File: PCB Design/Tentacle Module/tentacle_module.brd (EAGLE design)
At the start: 94 x 50.8 mm, 49 parts, among them IC1 5V, T1 NTD5867NL, T2 NTD5867NL, T3 NTD5867NL, T4 NTD5867NL, X3 RJ45-8X, X4 RJ45-8X

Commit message: Added the RJ45 connector
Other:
- outline, holes or cut-outs redrawn
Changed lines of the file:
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@@
 <board>
 <plain>
-<wire x1="0" y1="0" x2="93.98" y2="0" width="0.6096" layer="20"/>
+<wire x1="0" y1="0" x2="16.51" y2="0" width="0.6096" layer="20"/>
+<wire x1="16.51" y1="0" x2="38.1" y2="0" width="0.6096" layer="20"/>
+<wire x1="38.1" y1="0" x2="93.98" y2="0" width="0.6096" layer="20"/>
 <wire x1="93.98" y1="0" x2="93.98" y2="50.8" width="0.6096" layer="20"/>
 <wire x1="93.98" y1="50.8" x2="0" y2="50.8" width="0.6096" layer="20"/>
@@
 <hole x="80.01" y="3.175" drill="4.7625"/>
 <hole x="12.7" y="3.175" drill="4.7625"/>
+<wire x1="16.51" y1="0" x2="16.51" y2="21.59" width="0.4064" layer="20"/>
+<wire x1="16.51" y1="21.59" x2="38.1" y2="21.59" width="0.4064" layer="20"/>
+<wire x1="38.1" y1="21.59" x2="38.1" y2="0" width="0.4064" layer="20"/>
 </plain>
 <attributes>

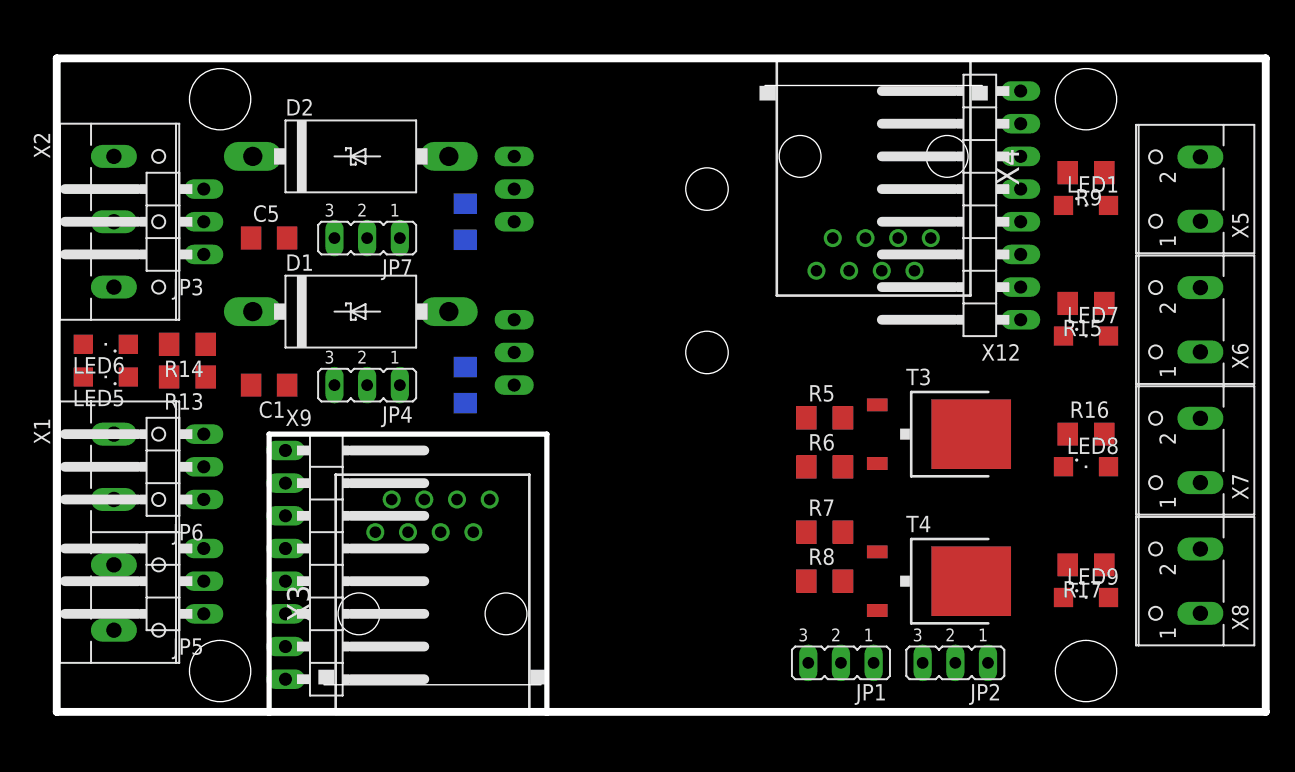
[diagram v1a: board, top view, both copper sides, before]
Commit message: Routed the RJ45 connector with side and top headers
Also added the accelerometer chip to the library
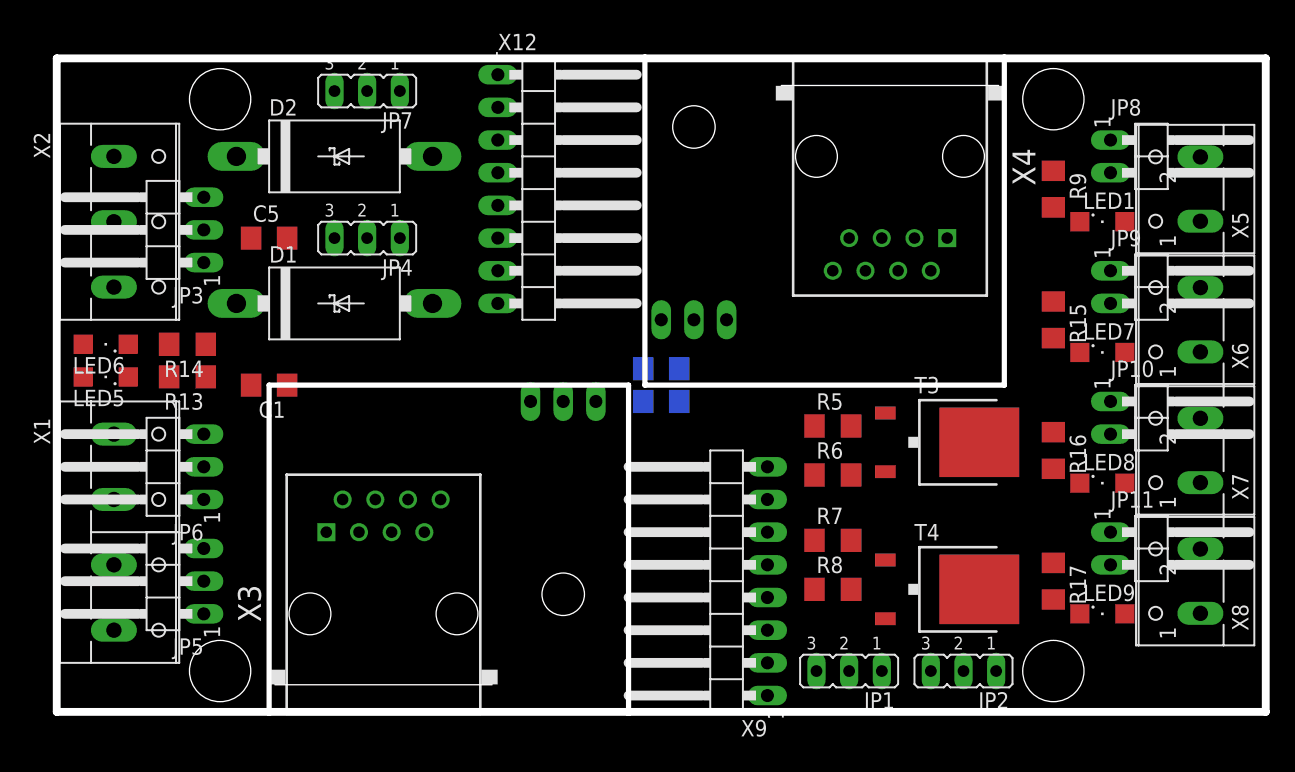
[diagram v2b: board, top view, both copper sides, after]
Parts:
- added JP10, JP11, JP8, JP9: (no value), CBLA_Test_bed_Library:1X02/90
- JP3, JP5, JP6: device pinhead:1X03/90 -> CBLA_Test_bed_Library:1X03/90
- X12, X9: device pinhead:1X08/90 -> CBLA_Test_bed_Library:1X08/90
- moved X12 33.0 mm to (38.1, 40.6), turned to 270 degrees
- moved X9 29.9 mm to (51.4, 10.2), turned to 90 degrees
- moved C4 19.1 mm to (47.0, 26.7), turned to 180 degrees
- moved C2 15.3 mm to (47.0, 24.1), turned to 0 degrees
- moved IC2 12.0 mm to (49.5, 34.3), turned to 0 degrees
- moved JP4 11.4 mm to (24.1, 36.8)
- moved JP7 11.4 mm to (24.1, 48.3)
- moved IC1 7.62 mm to (39.4, 20.3), turned to 180 degrees
- moved X3 3.81 mm to (25.4, 7.62)
- moved R15 2.84 mm to (77.5, 30.5), turned to 270 degrees
- moved R16 2.84 mm to (77.5, 20.3), turned to 270 degrees
- moved R17 2.84 mm to (77.5, 10.2), turned to 270 degrees
- moved R9 2.84 mm to (77.5, 40.6), turned to 270 degrees
- moved LED9 1.80 mm to (81.3, 7.62)
- moved LED7 1.80 mm to (81.3, 27.9)
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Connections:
- net +5V_HI-PWR: now also JP10.1, JP11.1, JP8.1, JP9.1
- net SMA1_OUT-: now also JP8.2
- net SMA2_OUT-: now also JP9.2
- net SMA3_OUT-: now also JP10.2
- net SMA4_OUT-: now also JP11.2
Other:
- outline, holes or cut-outs redrawn

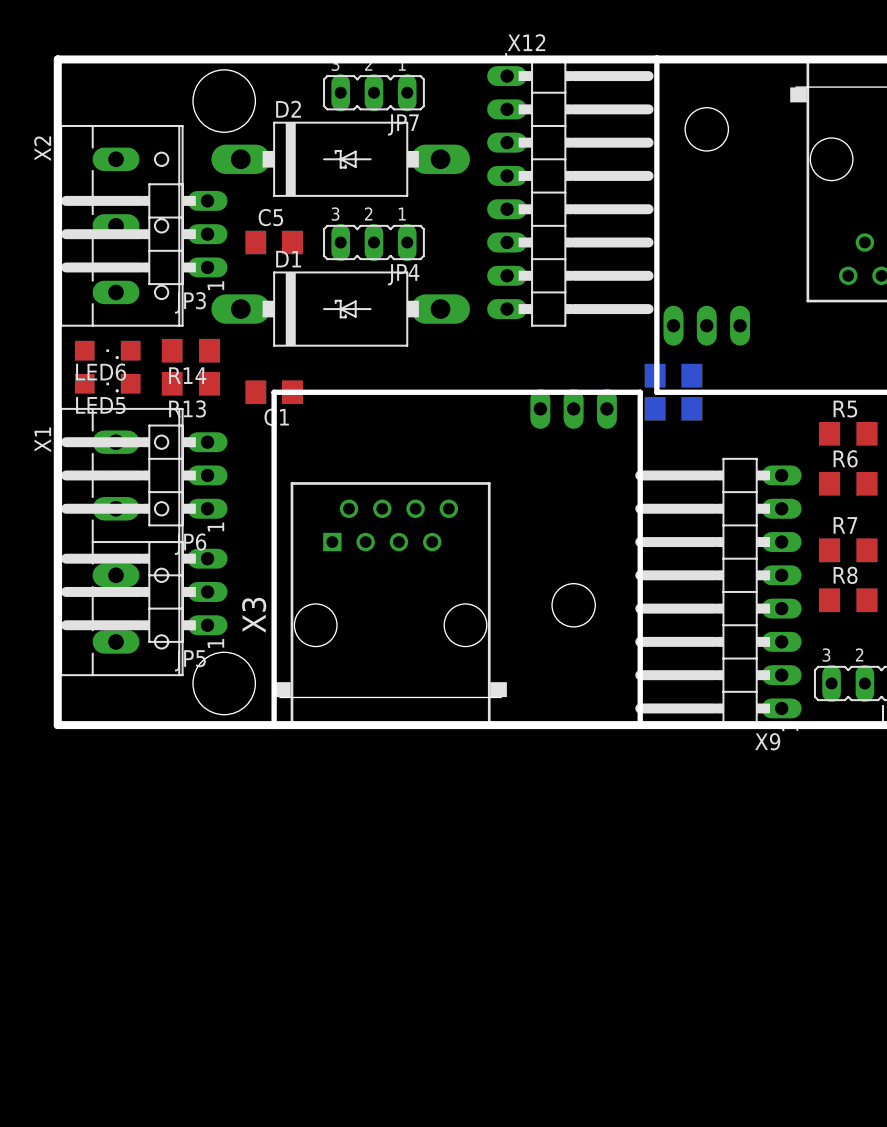
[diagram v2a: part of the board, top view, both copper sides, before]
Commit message: Changed location of the header to make it much easier to router
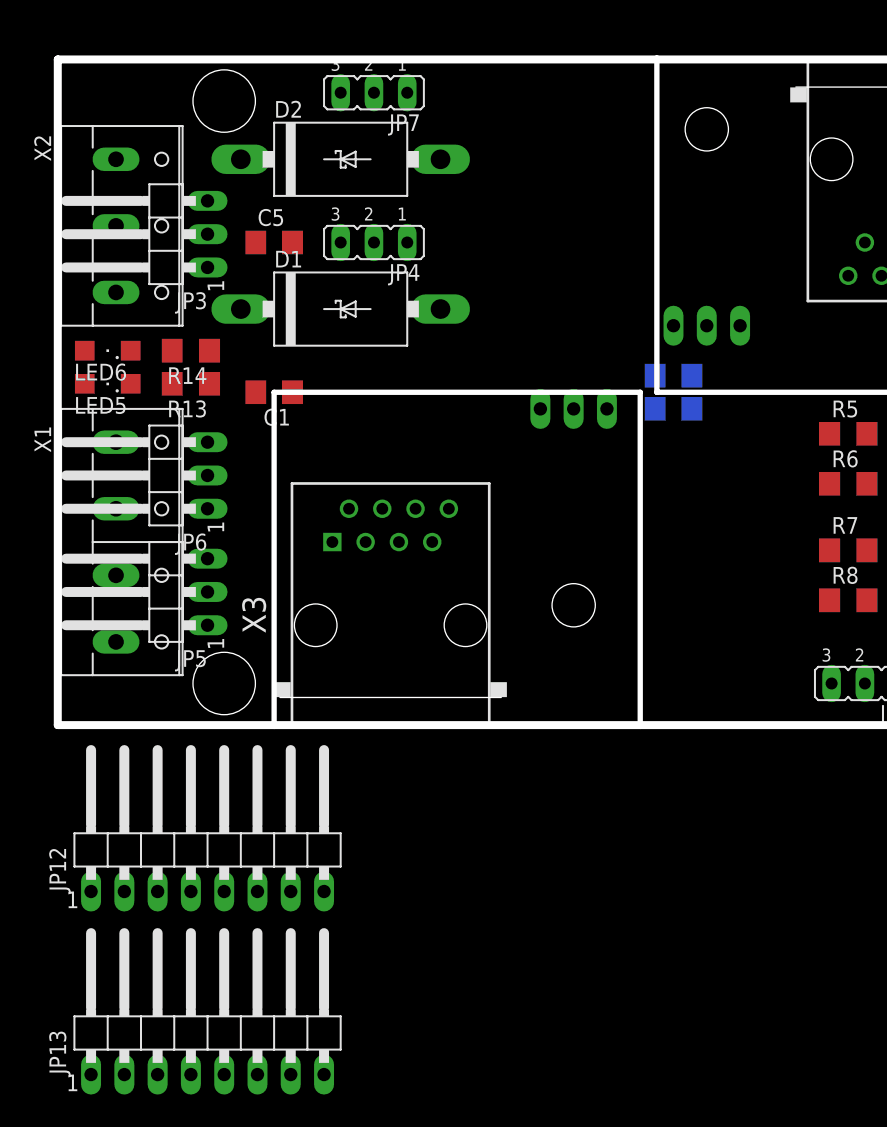
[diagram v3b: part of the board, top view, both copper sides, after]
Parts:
- removed X12, X9: (no value), CBLA_Test_bed_Library:1X08/90
- added JP12, JP13: (no value), CBLA_Test_bed_Library:1X08/90
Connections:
- net +3.3V: now also JP13.8; no longer X12.1
- net +5V: now also JP13.6; no longer X12.3
- net GND: now also JP13.7; no longer X12.2
- net IR1: now also JP12.4; no longer X9.5
- net IR2: now also JP12.3, JP13.5; no longer X12.4, X9.6
- net PWM1: now also JP12.8; no longer X9.1
- net PWM2: now also JP12.7; no longer X9.2
- net PWM3: now also JP12.6; no longer X9.3
- net PWM4: now also JP12.5; no longer X9.4
- net SCL: now also JP12.2, JP13.3; no longer X12.6, X9.7
- net SDA: now also JP12.1, JP13.4; no longer X12.5, X9.8
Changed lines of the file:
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@@
 <element name="T3" library="CBLA_Test_bed_Library" package="DPACK" value="NTD5867NL" x="69.215" y="20.955" rot="R270"/>
 <element name="T4" library="CBLA_Test_bed_Library" package="DPACK" value="NTD5867NL" x="69.215" y="9.525" rot="R270"/>
-<element name="X12" library="CBLA_Test_bed_Library" package="1X08/90" value="" x="38.1" y="40.64" rot="R270"/>
 <element name="X2" library="con-wago-508" package="W237-133" value="" x="5.08" y="38.1" rot="R270">
 <attribute name="OC_NEWARK" value="unknown" x="5.08" y="38.1" size="1.778" layer="27" rot="R270" display="off"/>
@@
 <attribute name="OC_FARNELL" value="unknown" x="87.63" y="10.16" size="1.778" layer="27" rot="R90" display="off"/>
 </element>
-<element name="X9" library="CBLA_Test_bed_Library" package="1X08/90" value="" x="51.435" y="10.16" rot="R90"/>
 <element name="X1" library="con-wago-508" package="W237-4P" value="" x="5.08" y="13.97" rot="R270">
 <attribute name="OC_NEWARK" value="unknown" x="5.08" y="13.97" size="1.778" layer="27" rot="R270" display="off"/>
@@
 <element name="JP10" library="CBLA_Test_bed_Library" package="1X02/90" value="" x="85.725" y="22.86" rot="R270"/>
 <element name="JP11" library="CBLA_Test_bed_Library" package="1X02/90" value="" x="85.725" y="12.7" rot="R270"/>
+<element name="JP12" library="CBLA_Test_bed_Library" package="1X08/90" value="" x="11.43" y="-8.89"/>
+<element name="JP13" library="CBLA_Test_bed_Library" package="1X08/90" value="" x="11.43" y="-22.86"/>
 </elements>
 <signals>
@@
 <contactref element="JP2" pad="3"/>
 <contactref element="JP1" pad="2"/>
-<contactref element="X12" pad="3"/>
+<contactref element="JP13" pad="6"/>
 <wire x1="48.39" y1="24.13" x2="66.675" y2="36.83" width="0" layer="19" extent="16-16"/>
 <wire x1="41.91" y1="24.13" x2="48.39" y2="24.13" width="0" layer="19" extent="16-16"/>
-<wire x1="34.29" y1="44.45" x2="41.91" y2="24.13" width="0" layer="19" extent="1-1"/>
 <wire x1="61.595" y1="3.175" x2="48.39" y2="24.13" width="0" layer="19" extent="16-16"/>
 <wire x1="67.945" y1="3.175" x2="61.595" y2="3.175" width="0" layer="19" extent="1-1"/>
 <wire x1="73.025" y1="3.175" x2="67.945" y2="3.175" width="0" layer="19" extent="1-1"/>
+<wire x1="15.24" y1="-26.67" x2="61.595" y2="3.175" width="0" layer="19" extent="1-1"/>
 </signal>
 <signal name="+3V3">
@@
 <contactref element="X3" pad="1"/>
 <contactref element="R3" pad="1"/>
-<contactref element="X9" pad="1"/>
-<wire x1="55.245" y1="1.27" x2="58.903" y2="22.225" width="0" layer="19" extent="16-16"/>
-<wire x1="20.955" y1="13.97" x2="55.245" y2="1.27" width="0" layer="19" extent="1-1"/>
+<contactref element="JP12" pad="8"/>
+<wire x1="20.955" y1="13.97" x2="58.903" y2="22.225" width="0" layer="19" extent="16-16"/>
+<wire x1="20.32" y1="-12.7" x2="20.955" y2="13.97" width="0" layer="19" extent="1-1"/>
 </signal>
 <signal name="PWM2">
 <contactref element="X3" pad="2"/>
 <contactref element="R4" pad="1"/>
-<contactref element="X9" pad="2"/>
-<wire x1="55.245" y1="3.81" x2="58.903" y2="13.335" width="0" layer="19" extent="16-16"/>
-<wire x1="22.225" y1="16.51" x2="55.245" y2="3.81" width="0" layer="19" extent="1-1"/>
+<contactref element="JP12" pad="7"/>
+<wire x1="22.225" y1="16.51" x2="58.903" y2="13.335" width="0" layer="19" extent="16-16"/>
+<wire x1="17.78" y1="-12.7" x2="22.225" y2="16.51" width="0" layer="19" extent="1-1"/>
 </signal>
 <signal name="PWM3">
 <contactref element="X3" pad="3"/>
-<contactref element="X9" pad="3"/>
 <contactref element="R6" pad="1"/>
-<wire x1="55.245" y1="6.35" x2="58.903" y2="18.415" width="0" layer="19" extent="1-1"/>
-<wire x1="23.495" y1="13.97" x2="55.245" y2="6.35" width="0" layer="19" extent="1-1"/>
+<contactref element="JP12" pad="6"/>
+<wire x1="23.495" y1="13.97" x2="58.903" y2="18.415" width="0" layer="19" extent="1-1"/>
+<wire x1="15.24" y1="-12.7" x2="23.495" y2="13.97" width="0" layer="19" extent="1-1"/>
 </signal>
 <signal name="PWM4">
 <contactref element="X3" pad="4"/>
-<contactref element="X9" pad="4"/>
 <contactref element="R8" pad="1"/>
-<wire x1="55.245" y1="8.89" x2="58.903" y2="9.525" width="0" layer="19" extent="1-1"/>
-<wire x1="24.765" y1="16.51" x2="55.245" y2="8.89" width="0" layer="19" extent="1-1"/>
+<contactref element="JP12" pad="5"/>
+<wire x1="24.765" y1="16.51" x2="58.903" y2="9.525" width="0" layer="19" extent="1-1"/>
+<wire x1="12.7" y1="-12.7" x2="24.765" y2="16.51" width="0" layer="19" extent="1-1"/>
 </signal>
 <signal name="IR1">
 <contactref element="X3" pad="5"/>
-<contactref element="X9" pad="5"/>
-<wire x1="26.035" y1="13.97" x2="55.245" y2="11.43" width="0" layer="19" extent="1-1"/>
+<contactref element="JP12" pad="4"/>
+<wire x1="10.16" y1="-12.7" x2="26.035" y2="13.97" width="0" layer="19" extent="1-1"/>
 </signal>
 <signal name="IR2">
 <contactref element="X3" pad="6"/>
 <contactref element="X4" pad="4"/>
-<contactref element="X9" pad="6"/>
-<contactref element="X12" pad="4"/>
-<wire x1="55.245" y1="13.97" x2="65.405" y2="34.29" width="0" layer="19" extent="1-1"/>
-<wire x1="27.305" y1="16.51" x2="55.245" y2="13.97" width="0" layer="19" extent="1-1"/>
-<wire x1="34.29" y1="41.91" x2="65.405" y2="34.29" width="0" layer="19" extent="1-1"/>
+<contactref element="JP12" pad="3"/>
+<contactref element="JP13" pad="5"/>
+<wire x1="27.305" y1="16.51" x2="65.405" y2="34.29" width="0" layer="19" extent="1-1"/>
+<wire x1="7.62" y1="-12.7" x2="27.305" y2="16.51" width="0" layer="19" extent="1-1"/>
+<wire x1="12.7" y1="-26.67" x2="7.62" y2="-12.7" width="0" layer="19" extent="1-1"/>
 </signal>
 <signal name="SCL">
 <contactref element="X3" pad="7"/>
 <contactref element="X4" pad="6"/>
-<contactref element="X9" pad="7"/>
-<contactref element="X12" pad="6"/>
-<wire x1="55.245" y1="16.51" x2="62.865" y2="34.29" width="0" layer="19" extent="1-1"/>
-<wire x1="28.575" y1="13.97" x2="55.245" y2="16.51" width="0" layer="19" extent="1-1"/>
-<wire x1="34.29" y1="36.83" x2="55.245" y2="16.51" width="0" layer="19" extent="1-1"/>
+<contactref element="JP12" pad="2"/>
+<contactref element="JP13" pad="3"/>
+<wire x1="28.575" y1="13.97" x2="62.865" y2="34.29" width="0" layer="19" extent="1-1"/>
+<wire x1="5.08" y1="-12.7" x2="28.575" y2="13.97" width="0" layer="19" extent="1-1"/>
+<wire x1="7.62" y1="-26.67" x2="5.08" y2="-12.7" width="0" layer="19" extent="1-1"/>
 </signal>
 <signal name="SDA">
 <contactref element="X3" pad="8"/>
 <contactref element="X4" pad="5"/>
-<contactref element="X9" pad="8"/>
-<contactref element="X12" pad="5"/>
-<wire x1="55.245" y1="19.05" x2="64.135" y2="36.83" width="0" layer="19" extent="1-1"/>
-<wire x1="29.845" y1="16.51" x2="55.245" y2="19.05" width="0" layer="19" extent="1-1"/>
-<wire x1="34.29" y1="39.37" x2="55.245" y2="19.05" width="0" layer="19" extent="1-1"/>
+<contactref element="JP12" pad="1"/>
+<contactref element="JP13" pad="4"/>
+<wire x1="29.845" y1="16.51" x2="64.135" y2="36.83" width="0" layer="19" extent="1-1"/>
+<wire x1="2.54" y1="-12.7" x2="29.845" y2="16.51" width="0" layer="19" extent="1-1"/>
+<wire x1="10.16" y1="-26.67" x2="2.54" y2="-12.7" width="0" layer="19" extent="1-1"/>
 </signal>
 <signal name="+3.3V">
 <contactref element="X4" pad="1"/>
-<contactref element="X12" pad="1"/>
-<wire x1="34.29" y1="49.53" x2="69.215" y2="36.83" width="0" layer="19" extent="1-1"/>
+<contactref element="JP13" pad="8"/>
+<wire x1="20.32" y1="-26.67" x2="69.215" y2="36.83" width="0" layer="19" extent="1-1"/>
 </signal>
 <signal name="GND">
@@
 <contactref element="JP5" pad="2"/>
 <contactref element="JP6" pad="2"/>
-<contactref element="X12" pad="2"/>
 <contactref element="X1" pad="2"/>
 <contactref element="X1" pad="3"/>
+<contactref element="JP13" pad="7"/>
 <wire x1="64.415" y1="23.235" x2="67.945" y2="34.29" width="0" layer="19" extent="16-16"/>
 <wire x1="64.415" y1="18.675" x2="64.415" y2="23.235" width="0" layer="19" extent="1-16"/>
@@
 <wire x1="64.415" y1="7.245" x2="64.415" y2="11.805" width="0" layer="19" extent="1-16"/>
 <wire x1="48.39" y1="26.67" x2="58.903" y2="22.225" width="0" layer="19" extent="1-16"/>
+<wire x1="45.59" y1="24.13" x2="48.39" y2="26.67" width="0" layer="19" extent="16-16"/>
 <wire x1="49.53" y1="30.48" x2="48.39" y2="26.67" width="0" layer="19" extent="16-16"/>
-<wire x1="45.59" y1="24.13" x2="48.39" y2="26.67" width="0" layer="19" extent="16-16"/>
 <wire x1="39.37" y1="24.13" x2="45.59" y2="24.13" width="0" layer="19" extent="16-16"/>
 <wire x1="29.21" y1="31.75" x2="39.37" y2="24.13" width="0" layer="19" extent="1-1"/>
 <wire x1="29.21" y1="43.18" x2="29.21" y2="31.75" width="0" layer="19" extent="1-1"/>
-<wire x1="34.29" y1="46.99" x2="29.21" y2="43.18" width="0" layer="19" extent="1-1"/>
 <wire x1="17.91" y1="36.83" x2="29.21" y2="31.75" width="0" layer="19" extent="1-1"/>
 <wire x1="11.43" y1="37.465" x2="17.91" y2="36.83" width="0" layer="19" extent="1-1"/>
 <wire x1="4.445" y1="38.1" x2="11.43" y2="37.465" width="0" layer="19" extent="1-1"/>
-<wire x1="15.11" y1="25.4" x2="17.91" y2="36.83" width="0" layer="19" extent="1-1"/>
-<wire x1="11.582" y1="26.035" x2="15.11" y2="25.4" width="0" layer="19" extent="1-1"/>
+<wire x1="11.582" y1="26.035" x2="11.43" y2="37.465" width="0" layer="19" extent="1-1"/>
+<wire x1="15.11" y1="25.4" x2="11.582" y2="26.035" width="0" layer="19" extent="1-1"/>
 <wire x1="11.43" y1="19.05" x2="11.582" y2="26.035" width="0" layer="19" extent="1-1"/>
 <wire x1="4.445" y1="16.51" x2="11.43" y2="19.05" width="0" layer="19" extent="1-1"/>
 <wire x1="4.445" y1="11.43" x2="4.445" y2="16.51" width="0" layer="19" extent="1-1"/>
 <wire x1="11.43" y1="10.16" x2="4.445" y2="11.43" width="0" layer="19" extent="1-1"/>
+<wire x1="17.78" y1="-26.67" x2="11.43" y2="10.16" width="0" layer="19" extent="1-1"/>
 </signal>
 <signal name="SMA1_OUT-">
